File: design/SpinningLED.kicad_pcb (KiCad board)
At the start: 2 copper layers, 67.5 x 67.5 mm, 26 parts, among them IC1 4069, IC2 4017, P1 +, P2 -, SW1 SW_PUSH

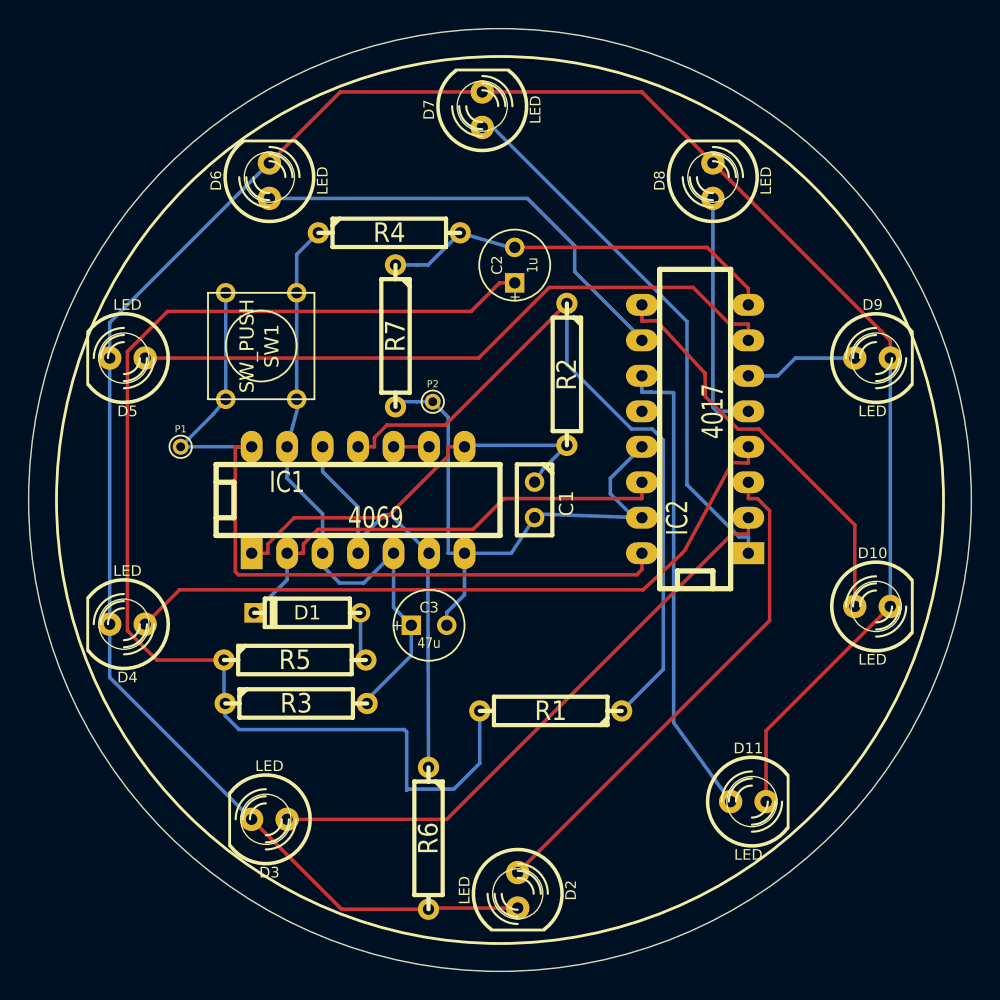
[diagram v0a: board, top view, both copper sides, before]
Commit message: Routed traces complete
Also removed R7 - 0 ohm resistor
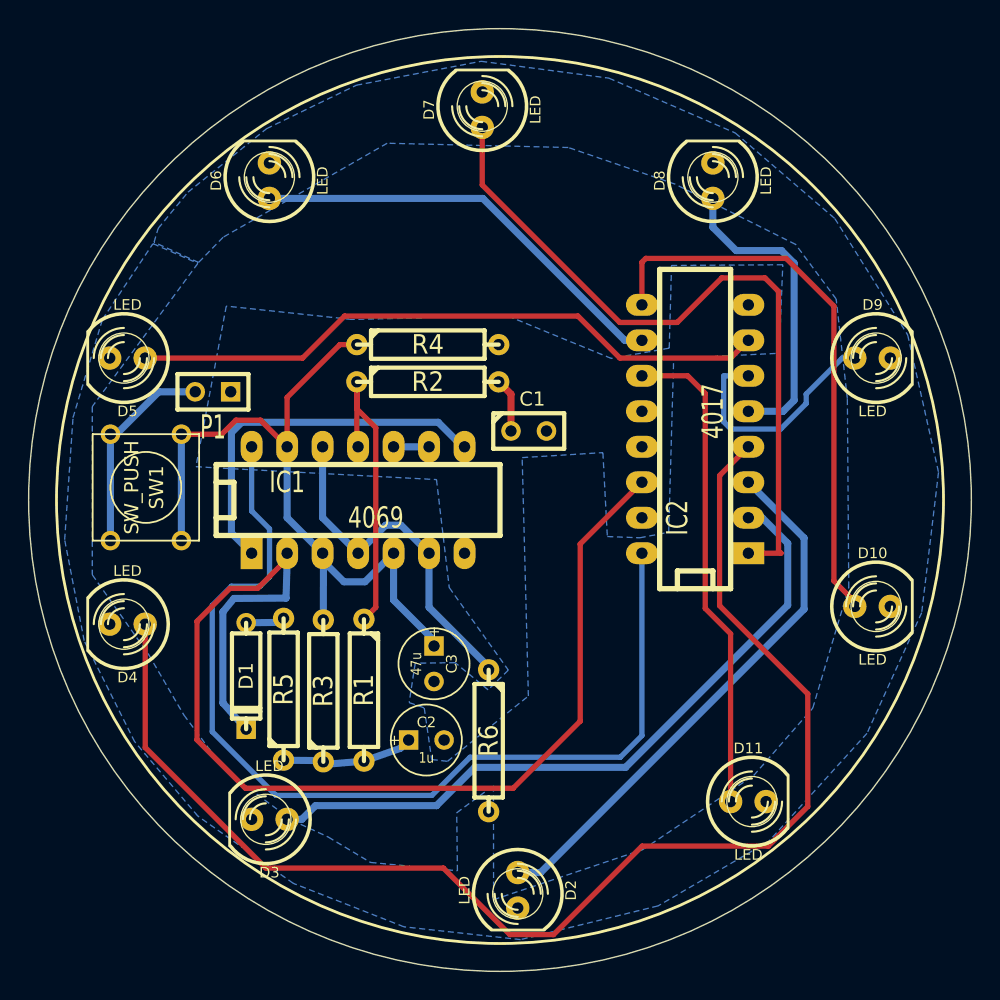
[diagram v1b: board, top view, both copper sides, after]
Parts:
- removed P2: -, PINTST
- removed R7: 0, R4
- D1: value 1N418 -> 1N4148
- P1: value + -> CONN_2; footprint PINTST -> SIL-2
- moved C2 34.6 mm to (133.2, 75.6), turned to 0 degrees
- moved R1 13.5 mm to (128.7, 72.0), turned to 270 degrees
- moved SW1 13.1 mm to (113.1, 57.5)
- moved R2 9.97 mm to (133.3, 50.0), turned to 0 degrees
- moved R4 8.46 mm to (133.3, 47.3)
- moved R6 8.21 mm to (137.6, 75.7)
- moved D1 6.30 mm to (120.3, 71.0), turned to 270 degrees
- moved C1 4.95 mm to (140.5, 53.5), turned to 0 degrees
- moved P1 4.57 mm to (117.9, 50.7), turned to 180 degrees
- moved C3 2.78 mm to (133.7, 70.1), turned to 270 degrees
- moved R5 2.25 mm to (122.9, 72.0), turned to 90 degrees
- moved R3 2.14 mm to (125.8, 72.1), turned to 90 degrees
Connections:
- C1 pad 1: N-000009 (its old number) -> N-0000018
- IC1 pad 1: N-000009 (its old number) -> N-0000017
- IC1 pad 8: N-000009 (its old number) -> N-0000017
- P1 pad 1: VCC -> GND
- R2 pad 2: N-000009 (its old number) -> N-0000018
- SW1 pad 2: VCC -> +9V
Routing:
- net /ResToLEDs: track 168.3 -> 0.00 mm
- net N-0000024: track 89.0 -> 9.48 mm
- net GND: track 71.2 -> 0.00 mm
- net N-000007: track 33.8 -> 84.2 mm
- net N-0000010: track 50.2 -> 94.8 mm
- net N-0000016: track 53.7 -> 22.6 mm
- net N-000009 (its old number): track 30.1 -> 0.00 mm
- net N-0000017: track 0.00 -> 27.0 mm
- net +9V: track 0.00 -> 14.9 mm
- net VCC: track 58.0 -> 71.3 mm
- net N-0000013: track 39.2 -> 52.3 mm
- net N-000002: track 29.3 -> 40.4 mm
- net N-0000023: track 44.8 -> 54.9 mm
- net N-000001: track 8.15 -> 17.1 mm
- net N-000009: track 42.6 -> 50.2 mm
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- added copper zone on B.Cu, net /ResToLEDs
- added copper zone on B.Cu, net GND
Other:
- net class Default: trace_width 0.254 -> 0.381

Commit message: V1 ready for OSH Park
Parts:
- added BH9VPC: VAL**, BH9VPC, F.Cu at (133.6, 60.5)
- moved C1 5.20 mm to (145.5, 52.1), turned to 270 degrees
- moved R6 3.17 mm to (140.8, 75.4)
- moved R5 3.02 mm to (125.9, 72.4)
- moved C3 2.99 mm to (136.7, 70.6)
- moved D1 2.83 mm to (117.4, 71.1)
- moved R3 2.63 mm to (128.4, 72.3)
- moved R1 2.25 mm to (130.9, 72.4)
- moved C2 1.68 mm to (134.8, 75.6)
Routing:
- net N-000007: track 84.2 -> 93.0 mm
- net N-000006: track 2.80 -> 8.64 mm
- net VCC: track 71.3 -> 76.3 mm
- net N-0000018: track 3.88 -> 7.53 mm
- net N-0000023: track 54.9 -> 58.4 mm
- net N-0000021: track 25.5 -> 27.4 mm
- net N-0000024: track 9.48 -> 8.35 mm
- net N-0000016: track 22.6 -> 23.2 mm
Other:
- board text added: "+"
- board text added: "Brooke Hedrick"
- board text added: "Spinning LED Schematic: Velleman mk152"
- board text added: "Spinning LED Schematic: Vellman mk152"

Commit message: SpinningLED v3
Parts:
- SW1: footprint SW_PUSH_SMALL -> SW_PUSH_SMALL_BTH
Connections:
- C1 pad 1: N-0000018 -> N-0000015
- C3 pad 1: N-0000023 -> +9V
- D10 pad 2: /ResToLEDs -> GND
- D11 pad 2: /ResToLEDs -> GND
- D2 pad 2: /ResToLEDs -> GND
- D3 pad 2: /ResToLEDs -> GND
- D4 pad 2: /ResToLEDs -> GND
- D5 pad 2: /ResToLEDs -> GND
- D6 pad 2: /ResToLEDs -> GND
- D7 pad 2: /ResToLEDs -> GND
- D8 pad 2: /ResToLEDs -> GND
- D9 pad 2: /ResToLEDs -> GND
- IC1 pad 1: N-0000017 -> N-0000015
- IC1 pad 13: N-0000023 -> +9V
- IC1 pad 3: N-0000023 -> +9V
- IC1 pad 5: N-0000023 -> +9V
- IC1 pad 8: N-0000017 -> N-0000015
- P1 pad 2: +9V -> VCC
- R2 pad 2: N-0000018 -> N-0000015
- R3 pad 2: N-0000023 -> +9V
- R4 pad 1: N-0000023 -> +9V
- R6 pad 2: /ResToLEDs -> GND
- SW1 pad 1: N-0000023 -> VCC
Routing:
- net N-0000023: track 58.4 -> 0.00 mm
- net +9V: track 14.9 -> 65.3 mm
- net N-0000015: track 0.00 -> 40.8 mm
- net N-0000017: track 27.0 -> 0.00 mm
- net VCC: track 76.3 -> 92.8 mm
- net N-0000018: track 7.53 -> 0.00 mm
- removed copper zone on B.Cu, net /ResToLEDs
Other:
- net class BigConnect added: clearance 0.254, trace_width 1.778, via_dia 0.889, via_drill 0.635
- board text added: "+9V-"
- board text added: "10n"
- board text removed: "+"
